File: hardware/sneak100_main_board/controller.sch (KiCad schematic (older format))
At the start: 17 parts, among them J13 Conn_02x05_Odd_Even, U9 STM32F405RGTx, Y1 8MHz

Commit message: Version 1.1 begin
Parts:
- added C33: 100nF, Capacitor_SMD:C_0603_1608Metric, symbol Device:C
- added SW5: SW_Push, Button_Switch_SMD:SW_Push_1P1T_NO_6x6mm_H9.5mm, symbol Switch:SW_Push
- JP1: footprint Connector_PinHeader_2.54mm:PinHeader_2x01_P2.54mm_Vertical -> Connector_PinHeader_2.54mm:PinHeader_1x03_P2.54mm_Vertical
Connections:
- net BLUETOOTH_STATUS is gone; now on net PROXIMITY_FL: U9.21 (PA5)
- net I2C3_SCL is gone; now on net LB_IN1: U9.41 (PA8)
- net I2C3_SDA is gone; now on net RF_IN2: U9.40 (PC9)
- net USER_LED_ERROR is gone; now on net USER_BUTTON_L: U9.51 (PC10)
- net USER_LED_RUN is gone; now on net LF_A: U9.50 (PA15)
- net BLUETOOTH_EN: now also U9.28 (PB2); no longer U9.20 (PA4)
- net GND: now also C33.2, SW5.1; no longer U9.28 (PB2)
- net LB_A: now also U9.56 (PB4); no longer U9.22 (PA6)
- net LB_B: now also U9.57 (PB5); no longer U9.23 (PA7)
- net LB_IN1: no longer U9.26 (PB0)
- net LB_IN2: now also U9.42 (PA9); no longer U9.27 (PB1)
- net LF_A: no longer U9.37 (PC6)
- net LF_B: now also U9.55 (PB3); no longer U9.38 (PC7)
- net LF_IN1: now also U9.43 (PA10); no longer U9.35 (PB14)
- net LF_IN2: now also U9.44 (PA11); no longer U9.36 (PB15)
- net PROXIMITY_FL: no longer U9.25 (PC5)
- net PROXIMITY_FR: now also U9.22 (PA6); no longer U9.57 (PB5)
- net PROXIMITY_LL: now also U9.20 (PA4); no longer U9.55 (PB3)
- net PROXIMITY_RR: now also U9.23 (PA7); no longer U9.56 (PB4)
- net RB_IN1: now also U9.37 (PC6); no longer U9.29 (PB10)
- net RB_IN2: now also U9.38 (PC7); no longer U9.30 (PB11)
- net RF_IN1: now also U9.39 (PC8); no longer U9.61 (PB8)
- net RF_IN2: no longer U9.62 (PB9)
- net RST: now also C33.1, SW5.2
- net USER_BUTTON_C: now also U9.52 (PC11); no longer U9.53 (PC12)
- net USER_BUTTON_L: no longer U9.52 (PC11)
- net USER_BUTTON_R: now also U9.53 (PC12); no longer U9.54 (PD2)
- new net BLUETOOTH_PWR: U9.26 (PB0)
- new net BLUETOOTH_ST: U9.27 (PB1)
- new net I2C1_SCL: U9.61 (PB8)
- new net I2C1_SDA: U9.62 (PB9)
- new net USART3_RX: U9.30 (PB11)
- new net USART3_TX: U9.29 (PB10)
- new net USER_LED_GREEN: U9.35 (PB14)
- new net USER_LED_YELLOW: U9.36 (PB15)
- no-connect marks 12 -> 10
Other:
- moved on the sheet: R13
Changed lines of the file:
@@
 L Device:R R?
 U 1 1 60060D9D
-P 9350 1650
+P 9850 1300
 AR Path="/60060D9D" Ref="R?"  Part="1"
 AR Path="/6004A52B/60060D9D" Ref="R?"  Part="1"
 AR Path="/6100FE40/60060D9D" Ref="R13"  Part="1"
-F 0 "R13" H 9420 1696 50  0000 L CNN
-F 1 "10k" H 9420 1605 50  0000 L CNN
-F 2 "Resistor_SMD:R_0603_1608Metric" V 9280 1650 50  0001 C CNN
-F 3 "~" H 9350 1650 50  0001 C CNN
-	1    9350 1650
-	1    0    0    -1
-$EndComp
-$Comp
-L power:+3.3V #PWR?
-U 1 1 60060DA4
-P 9350 1500
-AR Path="/60060DA4" Ref="#PWR?"  Part="1"
-AR Path="/6004A52B/60060DA4" Ref="#PWR?"  Part="1"
-AR Path="/6100FE40/60060DA4" Ref="#PWR089"  Part="1"
-F 0 "#PWR089" H 9350 1350 50  0001 C CNN
-F 1 "+3.3V" H 9365 1673 50  0000 C CNN
-F 2 "" H 9350 1500 50  0001 C CNN
-F 3 "" H 9350 1500 50  0001 C CNN
-	1    9350 1500
+F 0 "R13" H 9920 1346 50  0000 L CNN
+F 1 "10k" H 9920 1255 50  0000 L CNN
+F 2 "Resistor_SMD:R_0603_1608Metric" V 9780 1300 50  0001 C CNN
+F 3 "~" H 9850 1300 50  0001 C CNN
+	1    9850 1300
 	1    0    0    -1
 $EndComp
@@
 Text HLabel 4650 2600 2    50   Input ~ 0
 USART2_RX
-Text HLabel 4650 2900 2    50   Input ~ 0
+Text HLabel 4650 4400 2    50   Input ~ 0
 LB_A
-Text HLabel 4650 3000 2    50   Input ~ 0
+Text HLabel 4650 4500 2    50   Input ~ 0
 LB_B
-Text HLabel 4650 3100 2    50   BiDi ~ 0
-I2C3_SCL
-NoConn ~ 4650 3200
-NoConn ~ 4650 3300
-Text HLabel 4650 3800 2    50   Output ~ 0
-USER_LED_RUN
-Text HLabel 4650 4000 2    50   Output ~ 0
+Text HLabel 4650 4800 2    50   BiDi ~ 0
+I2C1_SCL
+Text HLabel 4650 5400 2    50   Output ~ 0
+USER_LED_GREEN
+Text HLabel 4650 3100 2    50   Output ~ 0
 LB_IN1
-Text HLabel 4650 4100 2    50   Output ~ 0
+Text HLabel 4650 3200 2    50   Output ~ 0
 LB_IN2
-Text HLabel 4650 4300 2    50   Input ~ 0
+Text HLabel 4650 2700 2    50   Input ~ 0
 PROXIMITY_LL
-Text HLabel 3250 4500 0    50   Input ~ 0
+Text HLabel 4650 2800 2    50   Input ~ 0
 PROXIMITY_FL
 Text HLabel 4650 2300 2    50   Input ~ 0
@@
 Text HLabel 4650 2400 2    50   Input ~ 0
 RB_B
-Text HLabel 4650 5000 2    50   Output ~ 0
+Text HLabel 3250 4600 0    50   Output ~ 0
 RB_IN1
-Text HLabel 4650 5100 2    50   Output ~ 0
+Text HLabel 3250 4700 0    50   Output ~ 0
 RB_IN2
-Text HLabel 4650 4800 2    50   Output ~ 0
+Text HLabel 3250 4800 0    50   Output ~ 0
 RF_IN1
-Text HLabel 4650 4900 2    50   Output ~ 0
+Text HLabel 3250 4900 0    50   Output ~ 0
 RF_IN2
 NoConn ~ 4650 5200
 NoConn ~ 4650 5300
-Text HLabel 4650 5400 2    50   Output ~ 0
+Text HLabel 4650 3300 2    50   Output ~ 0
 LF_IN1
-Text HLabel 4650 5500 2    50   Output ~ 0
+Text HLabel 4650 3400 2    50   Output ~ 0
 LF_IN2
 Text HLabel 3250 5300 0    50   Input ~ 0
@@
 Text HLabel 3250 4400 0    50   Input ~ 0
 BATTERY_SENSE
-Text HLabel 3250 4600 0    50   Input ~ 0
+Text HLabel 4650 3800 2    50   Input ~ 0
 LF_A
-Text HLabel 3250 4700 0    50   Input ~ 0
+Text HLabel 4650 4300 2    50   Input ~ 0
 LF_B
-Text HLabel 3250 4900 0    50   BiDi ~ 0
-I2C3_SDA
-Text HLabel 3250 5000 0    50   Output ~ 0
-USER_LED_ERROR
-Text HLabel 3250 5200 0    50   Input ~ 0
+Text HLabel 4650 4900 2    50   BiDi ~ 0
+I2C1_SDA
+Text HLabel 4650 5500 2    50   Output ~ 0
+USER_LED_YELLOW
+Text HLabel 3250 5100 0    50   Input ~ 0
 USER_BUTTON_C
-NoConn ~ 3250 5500
 Text Label 3250 2500 2    50   ~ 0
 BOOT0
-Text Label 4650 4200 0    50   ~ 0
-BOOT1
-Text Label 8700 1850 0    50   ~ 0
-BOOT1
-$Comp
-L power:GND #PWR090
-U 1 1 60F14427
-P 8650 1900
-F 0 "#PWR090" H 8650 1650 50  0001 C CNN
-F 1 "GND" H 8655 1727 50  0000 C CNN
-F 2 "" H 8650 1900 50  0001 C CNN
-F 3 "" H 8650 1900 50  0001 C CNN
-	1    8650 1900
-	1    0    0    -1
-$EndComp
-Wire Wire Line
-	8650 1900 8650 1850
-Wire Wire Line
-	8650 1850 8700 1850
 Text Label 3250 2300 2    50   ~ 0
 RST
-Wire Wire Line
-	9350 1800 9350 1850
-Wire Wire Line
-	9350 1850 9400 1850
-Text Label 9400 1850 0    50   ~ 0
+Text Label 9950 1500 0    50   ~ 0
 RST
 Text Label 6500 3050 2    50   ~ 0
 RST
-NoConn ~ 3250 5400
 Text GLabel 7000 3450 2    50   Input ~ 0
 ST-LINK_5V
@@
 Wire Wire Line
 	8650 1350 8700 1350
-Text HLabel 3250 5100 0    50   Input ~ 0
+Text HLabel 3250 5000 0    50   Input ~ 0
 USER_BUTTON_L
-Text HLabel 3250 3800 0    50   Input ~ 0
+Text HLabel 3250 5200 0    50   Input ~ 0
 USER_BUTTON_R
-NoConn ~ 4650 3400
-NoConn ~ 4650 3500
 $Comp
 L Jumper:Jumper_2_Open JP1
@@
 F 0 "JP1" H 6700 1735 50  0000 C CNN
 F 1 "Jumper_2_Open" H 6700 1644 50  0000 C CNN
-F 2 "Connector_PinHeader_2.54mm:PinHeader_2x01_P2.54mm_Vertical" H 6700 1500 50  0001 C CNN
+F 2 "Connector_PinHeader_2.54mm:PinHeader_1x03_P2.54mm_Vertical" H 6700 1500 50  0001 C CNN
 F 3 "~" H 6700 1500 50  0001 C CNN
 	1    6700 1500
 	1    0    0    -1
 $EndComp
-Text GLabel 6500 1500 0    50   Input ~ 0
+Text GLabel 6500 1500 0    50   Output ~ 0
 ST-LINK_5V
-Text HLabel 4650 2700 2    50   Output ~ 0
+Text HLabel 4650 4200 2    50   Output ~ 0
 BLUETOOTH_EN
-Text HLabel 4650 2800 2    50   Input ~ 0
-BLUETOOTH_STATUS
-NoConn ~ 3250 4800
-Text HLabel 4650 4500 2    50   Input ~ 0
+Text HLabel 4650 4100 2    50   Input ~ 0
+BLUETOOTH_ST
+Text HLabel 4650 2900 2    50   Input ~ 0
 PROXIMITY_FR
-Text HLabel 4650 4400 2    50   Input ~ 0
+Text HLabel 4650 3000 2    50   Input ~ 0
 PROXIMITY_RR
 $Comp
@@
 Text Notes 6550 2700 0    50   ~ 10
 ST-LINK V2
+NoConn ~ 4650 3500
+Text HLabel 4650 5000 2    50   Output ~ 0
+USART3_TX
+Text HLabel 4650 5100 2    50   Input ~ 0
+USART3_RX
+Text HLabel 4650 4000 2    50   Output ~ 0
+BLUETOOTH_PWR
+NoConn ~ 3250 4500
+NoConn ~ 3250 5400
+NoConn ~ 3250 5500
+NoConn ~ 3250 3800
+$Comp
+L Switch:SW_Push SW?
+U 1 1 617B7545
+P 9600 1500
+AR Path="/60E0491A/617B7545" Ref="SW?"  Part="1"
+AR Path="/6100FE40/617B7545" Ref="SW5"  Part="1"
+F 0 "SW5" H 9600 1785 50  0000 C CNN
+F 1 "SW_Push" H 9600 1694 50  0000 C CNN
+F 2 "Button_Switch_SMD:SW_Push_1P1T_NO_6x6mm_H9.5mm" H 9600 1700 50  0001 C CNN
+F 3 "~" H 9600 1700 50  0001 C CNN
+	1    9600 1500
+	1    0    0    -1
+$EndComp
+$Comp
+L power:+3.3V #PWR?
+U 1 1 617B7551
+P 9850 1150
+AR Path="/60E0491A/617B7551" Ref="#PWR?"  Part="1"
+AR Path="/6100FE40/617B7551" Ref="#PWR0117"  Part="1"
+F 0 "#PWR0117" H 9850 1000 50  0001 C CNN
+F 1 "+3.3V" H 9865 1323 50  0000 C CNN
+F 2 "" H 9850 1150 50  0001 C CNN
+F 3 "" H 9850 1150 50  0001 C CNN
+	1    9850 1150
+	1    0    0    -1
+$EndComp
+$Comp
+L power:GND #PWR?
+U 1 1 617B7557
+P 9350 1550
+AR Path="/60E0491A/617B7557" Ref="#PWR?"  Part="1"
+AR Path="/6100FE40/617B7557" Ref="#PWR0118"  Part="1"
+F 0 "#PWR0118" H 9350 1300 50  0001 C CNN
+F 1 "GND" H 9355 1377 50  0000 C CNN
+F 2 "" H 9350 1550 50  0001 C CNN
+F 3 "" H 9350 1550 50  0001 C CNN
+	1    9350 1550
+	1    0    0    -1
+$EndComp
+$Comp
+L Device:C C?
+U 1 1 617B755D
+P 9850 1700
+AR Path="/60E0491A/617B755D" Ref="C?"  Part="1"
+AR Path="/6100FE40/617B755D" Ref="C33"  Part="1"
+F 0 "C33" H 9965 1746 50  0000 L CNN
+F 1 "100nF" H 9965 1655 50  0000 L CNN
+F 2 "Capacitor_SMD:C_0603_1608Metric" H 9888 1550 50  0001 C CNN
+F 3 "~" H 9850 1700 50  0001 C CNN
+	1    9850 1700
+	1    0    0    -1
+$EndComp
+$Comp
+L power:GND #PWR?
+U 1 1 617B7563
+P 9850 1850
+AR Path="/60E0491A/617B7563" Ref="#PWR?"  Part="1"
+AR Path="/6100FE40/617B7563" Ref="#PWR0119"  Part="1"
+F 0 "#PWR0119" H 9850 1600 50  0001 C CNN
+F 1 "GND" H 9855 1677 50  0000 C CNN
+F 2 "" H 9850 1850 50  0001 C CNN
+F 3 "" H 9850 1850 50  0001 C CNN
+	1    9850 1850
+	1    0    0    -1
+$EndComp
+Wire Wire Line
+	9400 1500 9350 1500
+Wire Wire Line
+	9350 1500 9350 1550
+Wire Wire Line
+	9800 1500 9850 1500
+Wire Wire Line
+	9850 1500 9850 1550
+Wire Wire Line
+	9850 1500 9850 1450
+Connection ~ 9850 1500
+Wire Wire Line
+	9850 1500 9950 1500
 $EndSCHEMATC

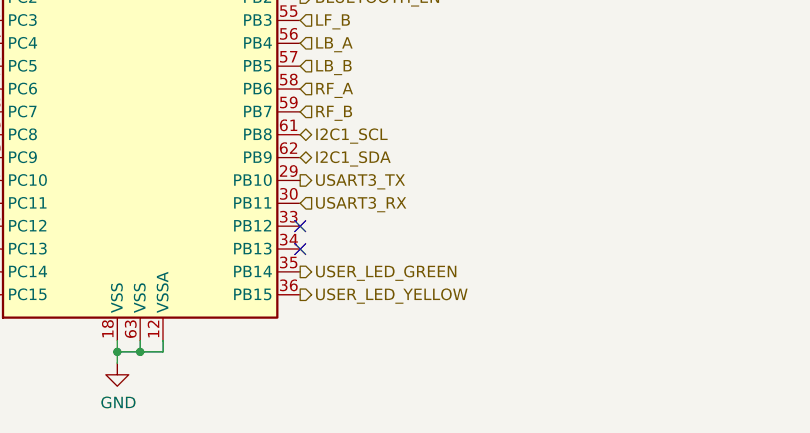
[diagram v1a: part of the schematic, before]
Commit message: uController routes in progress
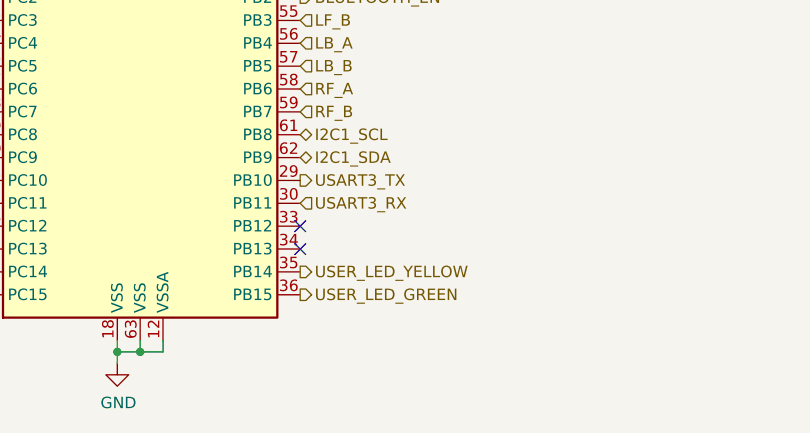
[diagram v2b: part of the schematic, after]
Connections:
- net USER_LED_GREEN: now also U9.36 (PB15); no longer U9.35 (PB14)
- net USER_LED_YELLOW: now also U9.35 (PB14); no longer U9.36 (PB15)
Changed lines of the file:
@@
 Text HLabel 4650 4800 2    50   BiDi ~ 0
 I2C1_SCL
-Text HLabel 4650 5400 2    50   Output ~ 0
+Text HLabel 4650 5500 2    50   Output ~ 0
 USER_LED_GREEN
 Text HLabel 4650 3100 2    50   Output ~ 0
@@
 Text HLabel 4650 4900 2    50   BiDi ~ 0
 I2C1_SDA
-Text HLabel 4650 5500 2    50   Output ~ 0
+Text HLabel 4650 5400 2    50   Output ~ 0
 USER_LED_YELLOW
 Text HLabel 3250 5100 0    50   Input ~ 0

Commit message: uController routes finish
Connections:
- net BLUETOOTH_EN: now also U9.23 (PA7); no longer U9.28 (PB2)
- net BLUETOOTH_PWR: now also U9.22 (PA6); no longer U9.26 (PB0)
- net BLUETOOTH_ST: now also U9.20 (PA4); no longer U9.27 (PB1)
- net PROXIMITY_FL: now also U9.26 (PB0); no longer U9.21 (PA5)
- net PROXIMITY_FR: now also U9.4 (PC15); no longer U9.22 (PA6)
- net PROXIMITY_LL: now also U9.27 (PB1); no longer U9.20 (PA4)
- net PROXIMITY_RR: now also U9.3 (PC14); no longer U9.23 (PA7)
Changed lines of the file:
@@
 Text HLabel 4650 3200 2    50   Output ~ 0
 LB_IN2
-Text HLabel 4650 2700 2    50   Input ~ 0
+Text HLabel 4650 4100 2    50   Input ~ 0
 PROXIMITY_LL
-Text HLabel 4650 2800 2    50   Input ~ 0
+Text HLabel 4650 4000 2    50   Input ~ 0
 PROXIMITY_FL
 Text HLabel 4650 2300 2    50   Input ~ 0
@@
 Text GLabel 6500 3450 0    50   Input ~ 0
 ST-LINK_5V
-Text Label 8700 1350 0    50   ~ 0
+Text Label 8650 1500 0    50   ~ 0
 BOOT0
 $Comp
 L power:GND #PWR087
 U 1 1 61068379
-P 8650 1400
-F 0 "#PWR087" H 8650 1150 50  0001 C CNN
-F 1 "GND" H 8655 1227 50  0000 C CNN
-F 2 "" H 8650 1400 50  0001 C CNN
-F 3 "" H 8650 1400 50  0001 C CNN
-	1    8650 1400
-	1    0    0    -1
-$EndComp
-Wire Wire Line
-	8650 1400 8650 1350
-Wire Wire Line
-	8650 1350 8700 1350
+P 8600 1550
+F 0 "#PWR087" H 8600 1300 50  0001 C CNN
+F 1 "GND" H 8605 1377 50  0000 C CNN
+F 2 "" H 8600 1550 50  0001 C CNN
+F 3 "" H 8600 1550 50  0001 C CNN
+	1    8600 1550
+	1    0    0    -1
+$EndComp
+Wire Wire Line
+	8600 1550 8600 1500
+Wire Wire Line
+	8600 1500 8650 1500
 Text HLabel 3250 5000 0    50   Input ~ 0
 USER_BUTTON_L
@@
 Text GLabel 6500 1500 0    50   Output ~ 0
 ST-LINK_5V
-Text HLabel 4650 4200 2    50   Output ~ 0
+Text HLabel 4650 3000 2    50   Output ~ 0
 BLUETOOTH_EN
-Text HLabel 4650 4100 2    50   Input ~ 0
+Text HLabel 4650 2700 2    50   Input ~ 0
 BLUETOOTH_ST
-Text HLabel 4650 2900 2    50   Input ~ 0
+Text HLabel 3250 5500 0    50   Input ~ 0
 PROXIMITY_FR
-Text HLabel 4650 3000 2    50   Input ~ 0
+Text HLabel 3250 5400 0    50   Input ~ 0
 PROXIMITY_RR
 $Comp
@@
 Text HLabel 4650 5100 2    50   Input ~ 0
 USART3_RX
-Text HLabel 4650 4000 2    50   Output ~ 0
+Text HLabel 4650 2900 2    50   Output ~ 0
 BLUETOOTH_PWR
-NoConn ~ 3250 4500
-NoConn ~ 3250 5400
-NoConn ~ 3250 5500
 NoConn ~ 3250 3800
 $Comp
@@
 Wire Wire Line
 	9850 1500 9950 1500
+NoConn ~ 4650 2800
+NoConn ~ 4650 4200
+NoConn ~ 3250 4500
 $EndSCHEMATC

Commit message: Version 1.1 probably finished
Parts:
- C32: footprint Capacitor_SMD:C_0805_2012Metric -> Capacitor_SMD:C_0603_1608Metric
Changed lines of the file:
@@
 encoding utf-8
 Sheet 7 7
-Title "Sneak100 Main Board V1.0"
-Date "August 2021"
+Title "Sneak100 Main Board V1.1"
+Date "September 2021"
 Rev ""
 Comp ""
@@
 F 0 "C32" H 9915 5446 50  0000 L CNN
 F 1 "4.7uF" H 9915 5355 50  0000 L CNN
-F 2 "Capacitor_SMD:C_0805_2012Metric" H 9838 5250 50  0001 C CNN
+F 2 "Capacitor_SMD:C_0603_1608Metric" H 9838 5250 50  0001 C CNN
 F 3 "~" H 9800 5400 50  0001 C CNN
 	1    9800 5400
